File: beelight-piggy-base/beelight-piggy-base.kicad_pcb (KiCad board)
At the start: 2 copper layers, 50 x 50 mm, 32 parts, among them J1 B_Le, J2 B_Ri, J3 USB_C_Receptacle_PowerOnly_6P, J4 WS2812_ext, J5 PROG, Q1 AO3400A, SW1 BOOT, U1 MCP73871, U2 BMA253, U3 TPS22917LDBV, U4 ADS1115IDGS, U6 TSOP382xx

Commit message: first final proto
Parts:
- removed SW1: BOOT, Button_Switch_SMD:SW_Tactile_SPST_NO_Straight_CK_PTS636Sx25SMTRLFS
- removed U4: ADS1115IDGS, Package_SO:TSSOP-10_3x3mm_P0.5mm
- added C1: 10µF, Capacitor_SMD:C_1210_3225Metric, F.Cu at (163.0, 78.2)
- added C10: 100n, Capacitor_SMD:C_0402_1005Metric, F.Cu at (173.7, 83.3)
- added C11: 100n, Capacitor_SMD:C_0402_1005Metric, F.Cu at (159.1, 112.1)
- added C12: 100n, Capacitor_SMD:C_0402_1005Metric, F.Cu at (141.2, 108.9)
- added C13: 100n, Capacitor_SMD:C_0402_1005Metric, F.Cu at (140.7, 82.1)
- added C14: 100n, Capacitor_SMD:C_0402_1005Metric, F.Cu at (147.4, 86.5)
- added C15: 100n, Capacitor_SMD:C_0402_1005Metric, F.Cu at (163.7, 104.6)
- added C16: 100n, Capacitor_SMD:C_0402_1005Metric, F.Cu at (161.6, 84.3)
- added C17: 100n, Capacitor_SMD:C_0402_1005Metric, F.Cu at (169.9, 108.7)
- added C18: 100n, Capacitor_SMD:C_0402_1005Metric, F.Cu at (167.7, 96.8)
- added C19: 100n, Capacitor_SMD:C_0402_1005Metric, F.Cu at (150.8, 112.4)
- added C2: 4.7µF, Capacitor_SMD:C_1210_3225Metric, F.Cu at (146.4, 90.6)
- added C20: 100n, Capacitor_SMD:C_0402_1005Metric, F.Cu at (136.5, 89.4)
- added C21: 100n, Capacitor_SMD:C_0402_1005Metric, F.Cu at (136.4, 101.7)
- added C22: 100µF, Capacitor_SMD:C_1210_3225Metric, F.Cu at (166.5, 85.7)
- added C3: 4.7µF, Capacitor_SMD:C_1210_3225Metric, F.Cu at (167.8, 105.0)
- added C4: 100n, Capacitor_SMD:C_0402_1005Metric, F.Cu at (178.2, 89.4)
- added C5: 100n, Capacitor_SMD:C_0402_1005Metric, F.Cu at (178.3, 100.7)
- added C6: 100n, Capacitor_SMD:C_0402_1005Metric, F.Cu at (146.9, 73.7)
- added C7: 100n, Capacitor_SMD:C_0402_1005Metric, F.Cu at (144.7, 97.5)
- added C8: 100n, Capacitor_SMD:C_0402_1005Metric, F.Cu at (146.9, 104.2)
- added C9: 100n, Capacitor_SMD:C_0402_1005Metric, F.Cu at (164.5, 73.4)
- added D17: LED_Small, LED_SMD:LED_0603_1608Metric, F.Cu at (132.4, 84.7)
- added D18: LED_Small, LED_SMD:LED_0603_1608Metric, F.Cu at (135.0, 82.4)
- added D19: LED_Small, LED_SMD:LED_0603_1608Metric, F.Cu at (137.4, 79.7)
- added F1: Polyfuse 1500mA, Fuse:Fuse_1812_4532Metric, F.Cu at (172.0, 87.8)
- added J7: DevSide, Connector_JST:JST_GH_SM02B-GHS-TB_1x02-1MP_P1.25mm_Horizontal, F.Cu at (145.0, 78.4)
- added J8: B_Ri, Connector_PinHeader_2.54mm:PinHeader_1x10_P2.54mm_Vertical, F.Cu at (157.4, 106.7)
- added J9: B_Le, Connector_PinHeader_2.54mm:PinHeader_1x10_P2.54mm_Vertical, F.Cu at (153.3, 106.7)
- added JP1: bypass_ws, Jumper:SolderJumper-2_P1.3mm_Open_RoundedPad1.0x1.5mm, F.Cu at (166.8, 80.5)
- added R1: 22k, Resistor_SMD:R_0805_2012Metric, F.Cu at (148.1, 82.4)
- added R10: 10k, Resistor_SMD:R_0805_2012Metric, F.Cu at (139.9, 86.6)
- added R11: 100R, Resistor_SMD:R_0805_2012Metric, F.Cu at (149.5, 95.4)
- added R12: 38R, Resistor_SMD:R_0805_2012Metric, F.Cu at (172.5, 104.9)
- added R13: 100k, Resistor_SMD:R_0805_2012Metric, F.Cu at (171.8, 99.5)
- added R14: 100R, Resistor_SMD:R_0805_2012Metric, F.Cu at (171.8, 97.6)
- added R15: 20k, Resistor_SMD:R_0805_2012Metric, F.Cu at (141.8, 86.6)
- added R16: 40k, Resistor_SMD:R_0805_2012Metric, F.Cu at (143.8, 86.6)
- added R17: 4k7, Resistor_SMD:R_0805_2012Metric, F.Cu at (141.7, 89.2)
- added R2: 22k, Resistor_SMD:R_0805_2012Metric, F.Cu at (149.6, 78.3)
- added R3: R470, Resistor_SMD:R_0805_2012Metric, F.Cu at (165.1, 82.1)
- added R5: 470R, Resistor_SMD:R_0805_2012Metric, F.Cu at (134.5, 86.0)
- added R6: 470R, Resistor_SMD:R_0805_2012Metric, F.Cu at (136.2, 84.8)
- added R7: 470R, Resistor_SMD:R_0805_2012Metric, F.Cu at (137.6, 83.4)
- added R8: 470R, Resistor_SMD:R_0805_2012Metric, F.Cu at (138.5, 104.3)
- added R9: 470R, Resistor_SMD:R_0805_2012Metric, F.Cu at (140.4, 104.3)
- added U5: VEML3328, beelight:VEML3328, F.Cu at (139.8, 100.5)
- J1, J2: footprint Connector_PinHeader_2.54mm:PinHeader_1x09_P2.54mm_Vertical -> Connector_PinHeader_2.54mm:PinHeader_1x10_P2.54mm_Vertical
- J3: footprint Connector_USB:USB_C_Receptacle_GCT_USB4105-xx-A_16P_TopMnt_Horizontal -> Connector_USB:USB_C_Receptacle_GCT_USB4125-xx-x-0190_6P_TopMnt_Horizontal
- J4: footprint Connector_Harwin:Harwin_M20-89003xx_1x03_P2.54mm_Horizontal -> Connector_JST:JST_GH_SM03B-GHS-TB_1x03-1MP_P1.25mm_Horizontal
- J5: value PROG -> Conn_01x07_Pin; footprint Connector_PinHeader_2.54mm:PinHeader_1x06_P2.54mm_Vertical_SMD_Pin1Right -> Connector_PinSocket_2.54mm:PinSocket_1x07_P2.54mm_Vertical
- TH1: footprint Resistor_SMD:R_2816_7142Metric_Pad3.20x4.45mm_HandSolder -> Resistor_SMD:R_0805_2012Metric
- moved J3 45.1 mm to (155.5, 72.2), turned to 180 degrees
- moved D20 36.1 mm to (176.4, 93.8)
- moved Q1 34.7 mm to (171.9, 93.9), turned to 90 degrees
- moved U1 30.8 mm to (138.8, 94.5), turned to 180 degrees
- moved U6 28.8 mm to (158.0, 80.3), turned to 180 degrees
- moved U2 22.2 mm to (144.1, 106.3)
- moved J5 16.8 mm to (132.1, 87.9)
- moved TH1 16.0 mm to (141.9, 91.2), turned to 0 degrees
- moved D12 15.1 mm to (176.5, 100.7)
- moved J4 14.2 mm to (169.5, 76.8), turned to 135 degrees
- moved D10 12.5 mm to (160.4, 113.4), turned to -135 degrees
- moved D11 12.1 mm to (171.4, 109.8), turned to -135 degrees
- moved D9 7.43 mm to (149.4, 113.7), turned to 135 degrees
- moved U3 6.85 mm to (167.0, 89.1)
- moved D4 5.50 mm to (148.7, 73.5)
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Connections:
- J1 pad 1: (no net) -> GND
- J1 pad 2: (no net) -> GND
- J1 pad 3: (no net) -> +5VP
- J1 pad 4: (no net) -> Net-(J1-SCLP)
- J1 pad 5: (no net) -> Net-(J1-SCL2)
- J1 pad 6: (no net) -> Net-(J1-SCL)
- J1 pad 7: (no net) -> Net-(J1-SDA)
- J1 pad 8: (no net) -> Net-(J1-TXD)
- J1 pad 9: (no net) -> Net-(J1-RXD)
- J2 pad 2: (no net) -> +3.3V
- J2 pad 3: (no net) -> Net-(J2-ADC)
- J2 pad 6: (no net) -> Net-(J2-RST)
- J2 pad 9: (no net) -> Net-(J2-BUZ)
- J5 pad 1: GND -> Net-(J1-EN)
- J5 pad 2: unconnected-(J5-Pin_2-Pad2) -> GND
- J5 pad 4: Net-(J1-Pin_2) -> Net-(J2-RST)
- J5 pad 5: Net-(J1-Pin_3) -> Net-(J1-RXD)
- J5 pad 6: unconnected-(J5-Pin_6-Pad6) -> Net-(J1-TXD)
- U2 pad 12: Net-(J1-Pin_5) -> Net-(J1-SCL)
- U2 pad 2: Net-(J1-Pin_4) -> Net-(J1-SDA)
- U3 pad 3: Net-(J1-Pin_6) -> Net-(J1-SCL2)
- U6 pad 1: Net-(J2-Pin_3) -> Net-(J1-SCLP)
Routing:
- net VLED: track 0.00 -> 178.1 mm, vias 0 -> 23
- net GND: track 0.00 -> 162.7 mm, vias 0 -> 26
- net Net-(J1-TXD): track 0.00 -> 86.1 mm, vias 0 -> 2
- net +5VP: track 0.00 -> 81.1 mm, vias 0 -> 4
- net VBUS: track 0.00 -> 71.8 mm, vias 0 -> 5
- net Net-(J1-RXD): track 0.00 -> 66.4 mm, vias 0 -> 3
- net +3.3V: track 0.00 -> 63.2 mm, vias 0 -> 4
- net Net-(J2-RST): track 0.00 -> 58.4 mm, vias 0 -> 1
- net Net-(D22-DOUT): track 0.00 -> 53.1 mm, vias 0 -> 2
- net Net-(J2-ADC): track 0.00 -> 50.1 mm, vias 0 -> 2
- net Net-(J1-SDA): track 0.00 -> 43.0 mm, vias 0 -> 1
- net Net-(J7-Pin_2): track 0.00 -> 26.4 mm, vias 0 -> 2
- net Net-(D15-DOUT): track 0.00 -> 25.9 mm
- net Net-(J1-EN): track 0.00 -> 22.9 mm
- net Net-(D5-DOUT): track 0.00 -> 21.9 mm
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- added copper zone on F.Cu, net GND
- added copper zone on B.Cu, net VLED
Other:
- outline, holes or cut-outs redrawn
- board text added: "ANTENNA KEEPOUT"

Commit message: pre jlc proto order
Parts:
- removed C10, C11, C12, C13, C14, C15, C16, C17, C18, C19, C20, C21, C4, C5, C6, C7, C8, C9: 100n, Capacitor_SMD:C_0402_1005Metric
- removed C2, C3: 4.7µF, Capacitor_SMD:C_1210_3225Metric
- removed J1, J9: B_Le, Connector_PinHeader_2.54mm:PinHeader_1x10_P2.54mm_Vertical
- removed J2, J8: B_Ri, Connector_PinHeader_2.54mm:PinHeader_1x10_P2.54mm_Vertical
- removed J5: Conn_01x07_Pin, Connector_PinSocket_2.54mm:PinSocket_1x07_P2.54mm_Vertical
- removed JP1: bypass_ws, Jumper:SolderJumper-2_P1.3mm_Open_RoundedPad1.0x1.5mm
- removed R10: 10k, Resistor_SMD:R_0805_2012Metric
- removed R15: 20k, Resistor_SMD:R_0805_2012Metric
- removed R16: 40k, Resistor_SMD:R_0805_2012Metric
- removed R17: 4k7, Resistor_SMD:R_0805_2012Metric
- removed R5, R6, R7, R8, R9: 470R, Resistor_SMD:R_0805_2012Metric
- removed U1: MCP73871, Package_DFN_QFN:QFN-20-1EP_4x4mm_P0.5mm_EP2.5x2.5mm
- added C23: 100nF, Capacitor_SMD:C_0402_1005Metric, F.Cu at (175.7, 94.2)
- added C25: 100nF, Capacitor_SMD:C_0402_1005Metric, F.Cu at (143.8, 82.4)
- added C26: 10uF, Capacitor_SMD:C_0805_2012Metric, F.Cu at (138.2, 88.5)
- added C27: 1uF, Capacitor_SMD:C_0402_1005Metric, F.Cu at (131.3, 93.0)
- added C28: 1uF, Capacitor_SMD:C_0603_1608Metric, F.Cu at (136.8, 98.7)
- added C29: 2.2uF, Capacitor_SMD:C_0603_1608Metric, F.Cu at (143.7, 91.7)
- added J10: USB C power only, Connector_USB:USB_C_Receptacle_GCT_USB4125-xx-x_6P_TopMnt_Horizontal, F.Cu at (155.2, 69.5)
- added J11: ExtWSSolderPads, Crystal:Resonator_SMD-3Pin_7.2x3.0mm_HandSoldering, B.Cu at (164.5, 76.2)
- added R18: 200k, Resistor_SMD:R_0402_1005Metric, F.Cu at (142.4, 83.8)
- added R19: 10k, Resistor_SMD:R_0402_1005Metric, F.Cu at (135.7, 92.7)
- added R20: 10k, Resistor_SMD:R_0402_1005Metric, F.Cu at (134.2, 94.1)
- added R21: 6.34k, Resistor_SMD:R_0402_1005Metric, F.Cu at (145.9, 82.3)
- added R22: 22.1k, Resistor_SMD:R_0402_1005Metric, F.Cu at (145.1, 80.0)
- added R23: 10k, Resistor_SMD:R_0402_1005Metric, F.Cu at (162.5, 94.4)
- added R24: 0R, Resistor_SMD:R_0402_1005Metric, F.Cu at (131.3, 87.7)
- added R25: 0R, Resistor_SMD:R_0402_1005Metric, F.Cu at (131.3, 85.7)
- added R26: 0R, Resistor_SMD:R_0402_1005Metric, F.Cu at (169.7, 82.4)
- added R27: 0R, Resistor_SMD:R_0402_1005Metric, F.Cu at (178.8, 92.2)
- added R4: 100k, Resistor_SMD:R_0402_1005Metric, F.Cu at (179.2, 96.3)
- added SW1: SW_Push, Button_Switch_SMD:SW_Push_SPST_NO_Alps_SKRK, B.Cu at (137.8, 77.5)
- added U4: rysta, beelight:rysta, F.Cu at (155.3, 95.4)
- added U7: MP2667, beelight:QFN-10_2x2mm_P0.5mm, F.Cu at (145.0, 86.7)
- added U8: BQ27421-G1, beelight:BGA-9_1.6x1.6mm_Layout3x3_P0.5mm, F.Cu at (135.8, 94.9)
- C1: value 10µF -> 10uF
- D1, D10, D11, D12, D13, D14, D15, D16, D2, D21, D22, D3, D4, D5, D6, D7, D8, D9: footprint LED_SMD:LED_WS2812B-2020_PLCC4_2.0x2.0mm -> EasyEDA_Lib:LED-SMD_6P-L2.2-W2.0_WS2816B-2020
- D17: value LED_Small -> BAT54C; footprint LED_SMD:LED_0603_1608Metric -> Package_TO_SOT_SMD:SOT-23
- D18, D19: value LED_Small -> BAT54J; footprint LED_SMD:LED_0603_1608Metric -> Diode_SMD:D_SOD-323F
- F1: footprint Fuse:Fuse_1812_4532Metric -> EasyEDA_Lib:F0805
- J3: value USB_C_Receptacle_PowerOnly_6P -> BatSolderPads; footprint Connector_USB:USB_C_Receptacle_GCT_USB4125-xx-x-0190_6P_TopMnt_Horizontal -> Diode_SMD:D_2114_3652Metric_Pad1.85x3.75mm_HandSolder; moved to B.Cu
- R1, R2: value 22k -> 5k1; footprint Resistor_SMD:R_0805_2012Metric -> Resistor_SMD:R_0402_1005Metric
- R11, R12, R13, R14, R3: footprint Resistor_SMD:R_0805_2012Metric -> Resistor_SMD:R_0402_1005Metric
- TH1: moved to B.Cu
- U2: footprint BMA253:LGA-12 -> beelight:LGA-12
- moved D19 43.3 mm to (178.3, 94.1), turned to 180 degrees
- moved J4 30.4 mm to (175.3, 106.6), turned to 45 degrees
- moved U5 29.8 mm to (168.4, 92.4), turned to 90 degrees
- moved J7 24.6 mm to (141.5, 102.7), turned to -45 degrees
- moved D15 22.9 mm to (149.1, 105.7), turned to 90 degrees
- moved D22 22.6 mm to (161.2, 84.8), turned to -90 degrees
- moved TH1 20.9 mm to (155.0, 74.9)
- moved R12 20.3 mm to (164.3, 86.3), turned to 0 degrees
- moved D20 19.2 mm to (157.5, 90.7), turned to 180 degrees
- moved C1 18.8 mm to (144.2, 77.5), turned to -135 degrees
- moved D18 18.5 mm to (143.5, 98.8), turned to 135 degrees
- moved R11 16.8 mm to (150.8, 78.7)
- moved R3 15.0 mm to (175.8, 92.7), turned to -90 degrees
- moved R13 14.2 mm to (163.8, 87.8), turned to 90 degrees
- moved D14 12.2 mm to (161.3, 105.9), turned to -90 degrees
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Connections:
- net Net-(J1-SCL) renamed SCL
- net Net-(J1-SDA) renamed SDA
- C22 pad 1: VLED -> Net-(D1-VDD)
- D1 pad 1: Net-(D1-DOUT) -> GND
- D1 pad 2: GND -> Net-(D1-DI)
- D1 pad 3: Net-(D1-DIN) -> Net-(D1-VDD)
- D1 pad 4: VLED -> Net-(D1-DO)
- D10 pad 1: Net-(D10-DOUT) -> Net-(D10-BI)
- D10 pad 2: GND -> Net-(D10-DI)
- D10 pad 3: Net-(D10-DIN) -> Net-(D1-VDD)
- D10 pad 4: VLED -> Net-(D10-DO)
- D11 pad 1: Net-(D11-DOUT) -> Net-(D10-BO)
- D11 pad 2: GND -> Net-(D10-DO)
- D11 pad 3: Net-(D10-DOUT) -> Net-(D1-VDD)
- D11 pad 4: VLED -> Net-(D11-DO)
- D12 pad 1: Net-(D12-DOUT) -> Net-(D11-BO)
- D12 pad 2: GND -> Net-(D11-DO)
- D12 pad 3: Net-(D11-DOUT) -> Net-(D1-VDD)
- D12 pad 4: VLED -> Net-(D12-DO)
- D13 pad 1: Net-(D13-DOUT) -> Net-(D12-BO)
- D13 pad 2: GND -> Net-(D12-DO)
- D13 pad 3: Net-(D12-DOUT) -> Net-(D1-VDD)
- D13 pad 4: VLED -> Net-(D13-DO)
- D14 pad 1: Net-(D14-DOUT) -> Net-(D13-BO)
- D14 pad 2: GND -> Net-(D13-DO)
- D14 pad 3: Net-(D13-DOUT) -> Net-(D1-VDD)
- D14 pad 4: VLED -> Net-(D14-DO)
- D15 pad 1: Net-(D15-DOUT) -> Net-(D14-BO)
- D15 pad 2: GND -> Net-(D14-DO)
- D15 pad 3: Net-(D14-DOUT) -> Net-(D1-VDD)
- D15 pad 4: VLED -> Net-(D15-DO)
- D16 pad 1: Net-(D16-DOUT) -> Net-(D15-BO)
- D16 pad 2: GND -> Net-(D15-DO)
- D16 pad 3: Net-(D15-DOUT) -> Net-(D1-VDD)
- D16 pad 4: VLED -> Net-(D16-DO)
- D17 pad 1: Net-(D17-K) -> WAKE
- D17 pad 2: VBUS -> Net-(U7-INT)
- D18 pad 1: Net-(D18-K) -> RST
- D18 pad 2: VBUS -> Net-(D18-A)
- D19 pad 1: Net-(D19-K) -> WS_DATA
- D19 pad 2: VBUS -> Net-(D19-A)
- D2 pad 1: Net-(D2-DOUT) -> Net-(D1-BO)
- D2 pad 2: GND -> Net-(D1-DO)
- D2 pad 3: Net-(D1-DOUT) -> Net-(D1-VDD)
- D2 pad 4: VLED -> Net-(D2-DO)
- D21 pad 1: Net-(D21-DOUT) -> Net-(D16-BO)
- D21 pad 2: GND -> Net-(D16-DO)
- D21 pad 3: Net-(D16-DOUT) -> Net-(D1-VDD)
- D21 pad 4: VLED -> Net-(D21-DO)
- D22 pad 1: Net-(D22-DOUT) -> Net-(D21-BO)
- D22 pad 2: GND -> Net-(D21-DO)
- D22 pad 3: Net-(D21-DOUT) -> Net-(D1-VDD)
- D22 pad 4: VLED -> Net-(D22-DO)
- D3 pad 1: Net-(D3-DOUT) -> Net-(D2-BO)
- D3 pad 2: GND -> Net-(D2-DO)
- D3 pad 3: Net-(D2-DOUT) -> Net-(D1-VDD)
- D3 pad 4: VLED -> Net-(D3-DO)
- D4 pad 1: Net-(D4-DOUT) -> Net-(D3-BO)
- D4 pad 2: GND -> Net-(D3-DO)
- D4 pad 3: Net-(D3-DOUT) -> Net-(D1-VDD)
- D4 pad 4: VLED -> Net-(D4-DO)
- D5 pad 1: Net-(D5-DOUT) -> Net-(D4-BO)
- D5 pad 2: GND -> Net-(D4-DO)
- D5 pad 3: Net-(D4-DOUT) -> Net-(D1-VDD)
- D5 pad 4: VLED -> Net-(D5-DO)
- D6 pad 1: Net-(D6-DOUT) -> Net-(D5-BO)
- D6 pad 2: GND -> Net-(D5-DO)
- D6 pad 3: Net-(D5-DOUT) -> Net-(D1-VDD)
- D6 pad 4: VLED -> Net-(D6-DO)
- D7 pad 1: Net-(D7-DOUT) -> Net-(D6-BO)
- D7 pad 2: GND -> Net-(D6-DO)
- D7 pad 3: Net-(D6-DOUT) -> Net-(D1-VDD)
- D7 pad 4: VLED -> Net-(D7-DO)
- D8 pad 1: Net-(D8-DOUT) -> Net-(D7-BO)
- D8 pad 2: GND -> Net-(D7-DO)
- D8 pad 3: Net-(D7-DOUT) -> Net-(D1-VDD)
- D8 pad 4: VLED -> Net-(D8-DO)
- D9 pad 1: Net-(D10-DIN) -> Net-(D8-BO)
- D9 pad 2: GND -> Net-(D8-DO)
- D9 pad 3: Net-(D8-DOUT) -> Net-(D1-VDD)
- D9 pad 4: VLED -> Net-(D10-DI)
- F1 pad 1: Net-(U3-VOUT) -> VLED
- F1 pad 2: VLED -> Net-(U3-VOUT)
- J4 pad 2: Net-(D22-DOUT) -> Net-(D22-DO)
- J7 pad 2: Net-(J7-Pin_2) -> BAT
- R1 pad 1: VBUS -> Net-(J10-CC1)
- R1 pad 2: Net-(J3-CC1) -> GND
- R12 pad 2: +5VP -> VLED
- R14 pad 1: Net-(J1-TXD) -> IR_TX
- R2 pad 1: VBUS -> GND
- R2 pad 2: Net-(J3-CC2) -> Net-(J10-CC2)
- R3 pad 1: Net-(J2-BUZ) -> Net-(D1-DI)
- R3 pad 2: Net-(D1-DIN) -> WS_DATA
- TH1 pad 1: Net-(U1-THERM) -> NTC
- U3 pad 3: Net-(J1-SCL2) -> Net-(D19-A)
- U6 pad 1: Net-(J1-SCLP) -> IR_RX
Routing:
- net Net-(D1-VDD): track 0.00 -> 289.4 mm
- net VLED: track 178.1 -> 62.0 mm, vias 23 -> 3
- net Net-(J1-TXD): track 86.1 -> 0.00 mm, vias 2 -> 0
- net WAKE: track 0.00 -> 70.7 mm, vias 0 -> 1
- net Net-(J1-RXD): track 66.4 -> 0.00 mm, vias 3 -> 0
- net Net-(D22-DO): track 0.00 -> 59.7 mm, vias 0 -> 2
- net Net-(J2-RST): track 58.4 -> 0.00 mm, vias 1 -> 0
- net BAT: track 0.00 -> 55.4 mm, vias 0 -> 1
- net SCL: track 19.6 -> 74.1 mm, vias 1 -> 3
- net Net-(D22-DOUT): track 53.1 -> 0.00 mm, vias 2 -> 0
- net RST: track 0.00 -> 50.6 mm, vias 0 -> 1
- net Net-(J2-ADC): track 50.1 -> 0.00 mm, vias 2 -> 0
- net VBUS: track 71.8 -> 24.6 mm, vias 5 -> 0
- net Net-(U8-SRX): track 0.00 -> 36.2 mm, vias 0 -> 3
- net IR_RX: track 0.00 -> 32.4 mm, vias 0 -> 1
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- added copper zone on B.Cu, net GND
- removed copper zone on B.Cu, net VLED
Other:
- board size 50 x 50 mm -> 55 x 55 mm

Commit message: last minor fixes pre order
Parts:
- added C30: 100nF, Capacitor_SMD:C_0402_1005Metric, F.Cu at (148.0, 98.0)
- added C31: 100nF, Capacitor_SMD:C_0402_1005Metric, F.Cu at (146.2, 95.7)
- added C32: 100nF, Capacitor_SMD:C_0402_1005Metric, F.Cu at (167.4, 91.6)
- moved U6 13.0 mm to (170.3, 74.9), turned to 150 degrees
- moved R11 8.24 mm to (159.1, 78.9)
- moved R23 1.05 mm to (161.8, 93.7)
- moved C28 0.27 mm to (136.6, 98.9)
- moved R2 0.23 mm to (153.3, 74.6)
- moved R1 0.23 mm to (157.0, 74.6)
- moved U5 0.20 mm to (168.5, 92.2)
- moved R19 0.17 mm to (135.9, 92.7)
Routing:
- net IR_RX: track 32.4 -> 47.6 mm, vias 1 -> 2
- net Net-(D1-VDD): track 289.4 -> 302.9 mm, vias 0 -> 2
- net BAT: track 55.4 -> 68.2 mm
- net GND: track 188.7 -> 180.5 mm, vias 22 -> 76
- net Net-(U6-Vs): track 1.70 -> 9.75 mm, vias 0 -> 1
- net +3.3V: track 70.0 -> 73.5 mm
- net SDA: track 68.2 -> 66.6 mm
- net Net-(D2-DO): track 10.1 -> 11.0 mm
- net Net-(U8-SRX): track 36.2 -> 37.1 mm
- net Net-(D2-BO): track 10.7 -> 11.5 mm
- net VLED: track 62.0 -> 61.2 mm
- net IR_TX: track 20.7 -> 21.3 mm
- net Net-(R19-Pad1): track 12.6 -> 13.2 mm
- net Net-(D13-BO): track 11.6 -> 11.1 mm

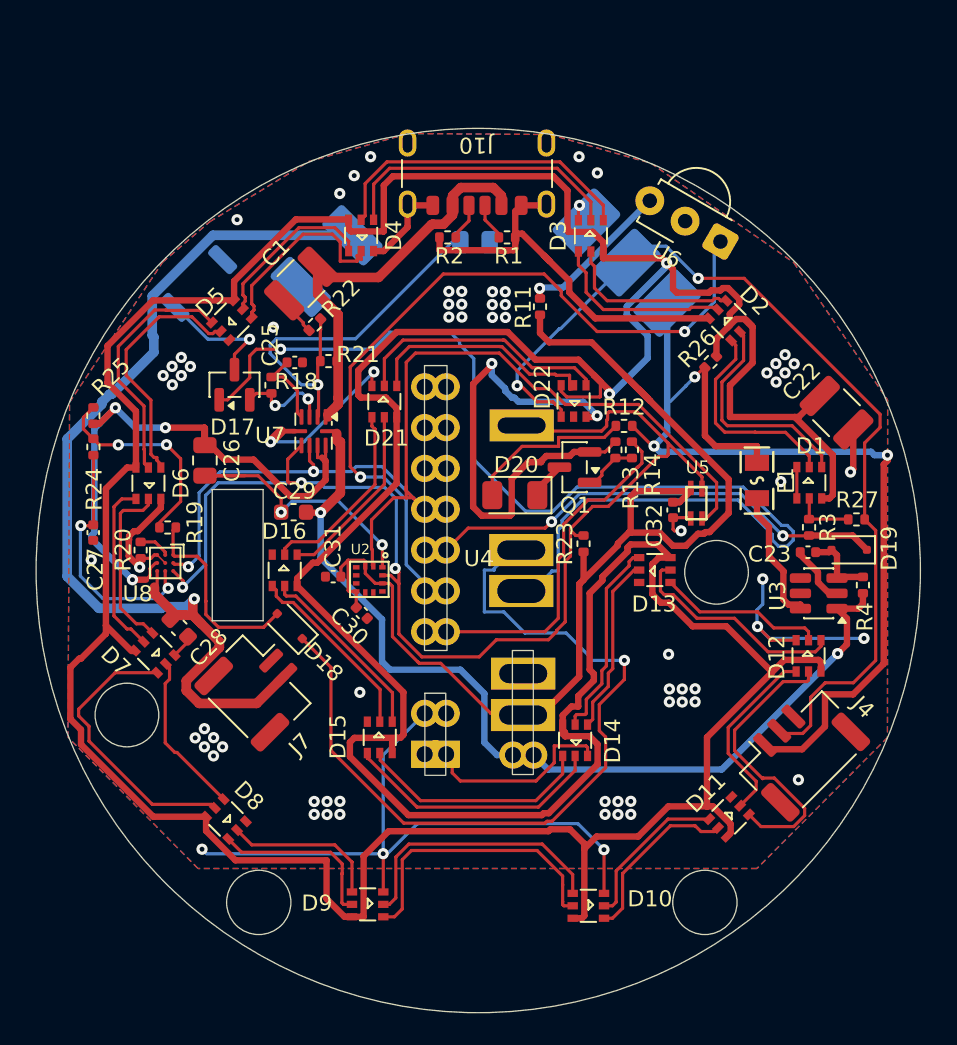
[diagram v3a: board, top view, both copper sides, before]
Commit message: more minor minor fixes pre proto order
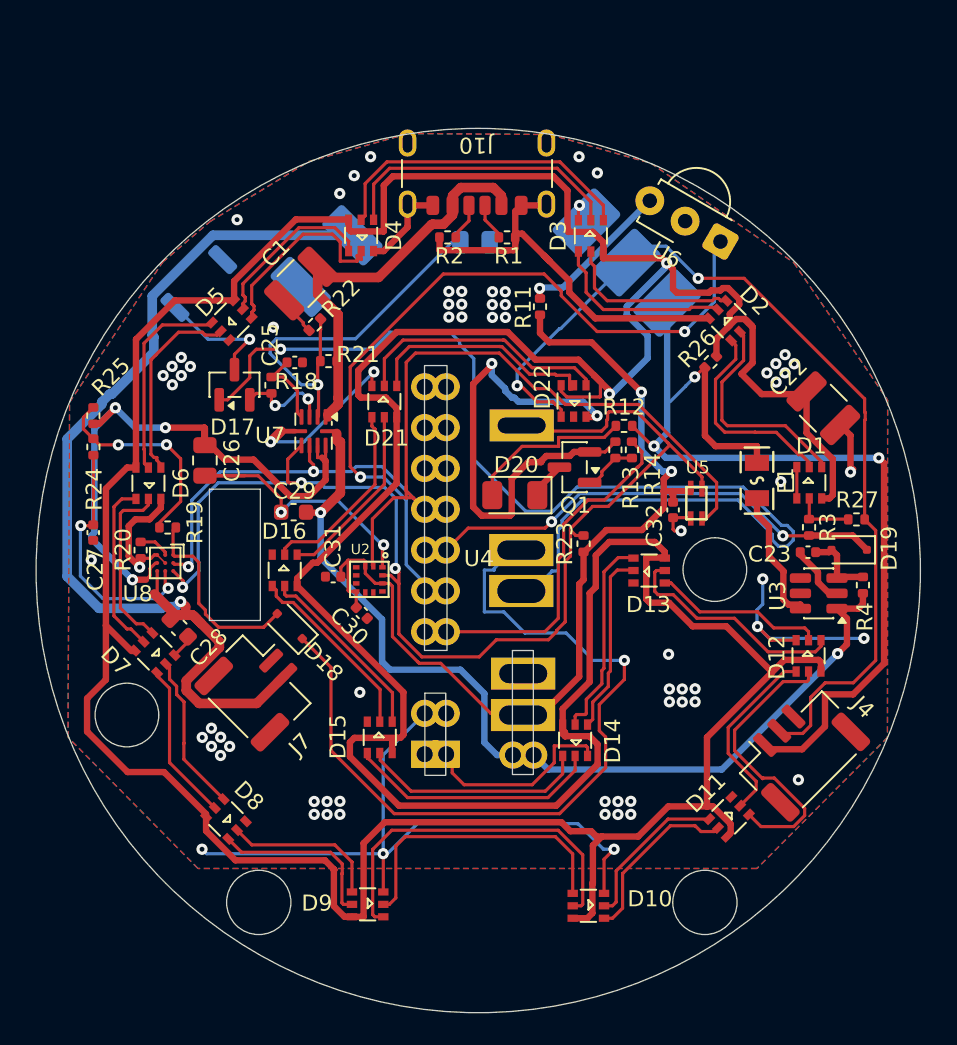
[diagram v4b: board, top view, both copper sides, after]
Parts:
- moved C22 0.87 mm to (176.7, 85.2)
- moved D13 0.36 mm to (165.9, 95.3)
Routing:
- net +3.3V: track 73.5 -> 57.9 mm, vias 0 -> 2
- net Net-(D7-DO): track 17.6 -> 9.90 mm
- net Net-(D10-DI): track 17.8 -> 22.7 mm
- net Net-(D1-VDD): track 302.9 -> 298.1 mm
- net Net-(D5-BO): track 15.4 -> 12.1 mm
- net Net-(D5-DO): track 15.4 -> 12.6 mm
- net BAT: track 68.2 -> 65.8 mm
- net GND: track 180.5 -> 182.7 mm
- net Net-(D22-DO): track 59.6 -> 57.4 mm
- net Net-(D10-BI): track 16.8 -> 18.3 mm
- net VLED: track 61.2 -> 60.7 mm
- net Net-(U6-Vs): track 9.75 -> 9.17 mm
- net IR_RX: track 47.6 -> 47.0 mm
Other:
- outline, holes or cut-outs redrawn

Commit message: tius feedback
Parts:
- moved C22 1.05 mm to (176.5, 84.2)
- moved U6 0.42 mm to (170.5, 74.5)
- moved R4 0.29 mm to (179.0, 96.5)
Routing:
- net Net-(D22-DO): track 57.4 -> 67.5 mm, vias 2 -> 4
- net Net-(D17-Pad3): track 6.95 -> 12.6 mm, vias 1 -> 2
- net GND: track 182.7 -> 187.2 mm
- net +5VP: track 57.6 -> 61.7 mm
- net +3.3V: track 57.9 -> 61.8 mm
- net RST: track 50.1 -> 53.4 mm
- net Net-(U8-VDD): track 15.7 -> 18.2 mm
- net IR_RX: track 47.0 -> 49.1 mm, vias 2 -> 3
- net Net-(D1-VDD): track 298.1 -> 300.1 mm
- net VLED: track 60.7 -> 58.7 mm
- net Net-(U6-Vs): track 9.17 -> 10.6 mm, vias 1 -> 2
- net BAT: track 65.8 -> 66.9 mm, vias 1 -> 2
- net IR_TX: track 21.3 -> 22.3 mm
- net SCL: track 74.1 -> 74.9 mm
- net Net-(U8-SRX): track 37.1 -> 36.4 mm
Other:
- outline, holes or cut-outs redrawn
- board text added: "+"
- board text added: "+ + + +"
- board text added: "+ Bat –"
- board text added: "-"
- board text added: "- - - -"
- board text added: "BAT"
- board text added: "BTN"
- board text added: "Btn"
- board text added: "DO"
- board text added: "ExtWS"
- board text added: "GND"
- board text added: "TSOP"
- board text added: "VCC"
- board text added: "WS ext"

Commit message: tius feedback 2
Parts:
- moved J4 0.97 mm to (176.1, 107.1), turned to 60 degrees
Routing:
- net VLED: track 58.7 -> 61.9 mm
- net Net-(D22-DO): track 67.5 -> 69.7 mm
- net GND: vias 76 -> 77
